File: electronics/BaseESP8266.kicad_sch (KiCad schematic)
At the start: 15 parts, among them P1 CONN_01X09, P2 CONN_01X09, SW1 Reset, T1 CONN_01X01, T2 CONN_01X01, U1 ESP-13-WROOM-02

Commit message: V2 Board needs: final traces, silkscreen and DRC
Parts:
- D5, D6: footprint mcqn-kicad-lib:LED_SMD_WL-SMSW_side-emitting -> LED_SMD:LED_0805_2012Metric_Pad1.15x1.40mm_HandSolder
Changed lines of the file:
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@@
       (effects (font (size 1.27 1.27)))
     )
-    (property "Footprint" "mcqn-kicad-lib:LED_SMD_WL-SMSW_side-emitting" (at 248.92 91.44 0)
+    (property "Footprint" "LED_SMD:LED_0805_2012Metric_Pad1.15x1.40mm_HandSolder" (at 248.92 91.44 0)
       (effects (font (size 1.27 1.27)) hide)
     )
@@
       (project "MyBikesGotLED"
         (path "/ea56fda8-6f8e-4826-a040-5c9b3e8e5cfa/00000000-0000-0000-0000-00005f8dad46"
-          (reference "D6") (unit 1) (value "LED") (footprint "mcqn-kicad-lib:LED_SMD_WL-SMSW_side-emitting")
+          (reference "D6") (unit 1) (value "LED") (footprint "LED_SMD:LED_0805_2012Metric_Pad1.15x1.40mm_HandSolder")
         )
       )
@@
       (effects (font (size 1.27 1.27)))
     )
-    (property "Footprint" "mcqn-kicad-lib:LED_SMD_WL-SMSW_side-emitting" (at 237.49 91.44 0)
+    (property "Footprint" "LED_SMD:LED_0805_2012Metric_Pad1.15x1.40mm_HandSolder" (at 237.49 91.44 0)
       (effects (font (size 1.27 1.27)) hide)
     )
@@
       (project "MyBikesGotLED"
         (path "/ea56fda8-6f8e-4826-a040-5c9b3e8e5cfa/00000000-0000-0000-0000-00005f8dad46"
-          (reference "D5") (unit 1) (value "LED") (footprint "mcqn-kicad-lib:LED_SMD_WL-SMSW_side-emitting")
+          (reference "D5") (unit 1) (value "LED") (footprint "LED_SMD:LED_0805_2012Metric_Pad1.15x1.40mm_HandSolder")
         )
       )

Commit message: V2 schematic - Battery management updates
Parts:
- renumbered C2 to C9, D5 to D1, D6 to D2, P1 to P3, P2 to P4, R9 to R12, R1 to R13, R2 to R14, R7 to R15, R8 to R16, R10 to R17, U1 to U4
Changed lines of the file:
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@@
-(kicad_sch (version 20221004) (generator eeschema)
+(kicad_sch (version 20221110) (generator eeschema)
   (paper "A4")
   (junction (at 144.78 57.15) (diameter 0) (color 0 0 0 0)
@@
   (symbol (lib_id "Device:R") (at 261.62 96.52 180) (unit 1)
     (in_bom yes) (on_board yes) (dnp no)
-    (property "Reference" "R10" (at 259.588 96.52 90)
+    (property "Reference" "R17" (at 259.588 96.52 90)
       (effects (font (size 1.27 1.27)))
     )
@@
       (project "MyBikesGotLED"
         (path "/ea56fda8-6f8e-4826-a040-5c9b3e8e5cfa/00000000-0000-0000-0000-00005f8dad46"
-          (reference "R10") (unit 1) (value "R10k") (footprint "Resistor_SMD:R_0603_1608Metric_Pad1.05x0.95mm_HandSolder")
+          (reference "R17") (unit 1) (value "R10k") (footprint "Resistor_SMD:R_0603_1608Metric_Pad1.05x0.95mm_HandSolder")
         )
       )
@@
   (symbol (lib_id "Device:C") (at 273.05 96.52 0) (unit 1)
     (in_bom yes) (on_board yes) (dnp no)
-    (property "Reference" "C2" (at 266.6492 96.52 90)
+    (property "Reference" "C9" (at 266.6492 96.52 90)
       (effects (font (size 1.27 1.27)))
     )
@@
       (project "MyBikesGotLED"
         (path "/ea56fda8-6f8e-4826-a040-5c9b3e8e5cfa/00000000-0000-0000-0000-00005f8dad46"
-          (reference "C2") (unit 1) (value "C47nF") (footprint "Capacitor_SMD:C_0603_1608Metric_Pad1.05x0.95mm_HandSolder")
+          (reference "C9") (unit 1) (value "C47nF") (footprint "Capacitor_SMD:C_0603_1608Metric_Pad1.05x0.95mm_HandSolder")
         )
       )
@@
   (symbol (lib_id "Device:R") (at 144.78 50.8 0) (unit 1)
     (in_bom yes) (on_board yes) (dnp no)
-    (property "Reference" "R9" (at 146.558 49.6316 0)
+    (property "Reference" "R12" (at 146.558 49.6316 0)
       (effects (font (size 1.27 1.27)) (justify left))
     )
@@
       (project "MyBikesGotLED"
         (path "/ea56fda8-6f8e-4826-a040-5c9b3e8e5cfa/00000000-0000-0000-0000-00005f8dad46"
-          (reference "R9") (unit 1) (value "R560") (footprint "Resistor_SMD:R_0603_1608Metric_Pad1.05x0.95mm_HandSolder")
+          (reference "R12") (unit 1) (value "R560") (footprint "Resistor_SMD:R_0603_1608Metric_Pad1.05x0.95mm_HandSolder")
         )
       )
@@
   (symbol (lib_id "Device:R") (at 248.92 101.6 180) (unit 1)
     (in_bom yes) (on_board yes) (dnp no)
-    (property "Reference" "R8" (at 246.888 101.6 90)
+    (property "Reference" "R16" (at 246.888 101.6 90)
       (effects (font (size 1.27 1.27)))
     )
@@
       (project "MyBikesGotLED"
         (path "/ea56fda8-6f8e-4826-a040-5c9b3e8e5cfa/00000000-0000-0000-0000-00005f8dad46"
-          (reference "R8") (unit 1) (value "R560") (footprint "Resistor_SMD:R_0603_1608Metric_Pad1.05x0.95mm_HandSolder")
+          (reference "R16") (unit 1) (value "R560") (footprint "Resistor_SMD:R_0603_1608Metric_Pad1.05x0.95mm_HandSolder")
         )
       )
@@
   (symbol (lib_id "Device:R") (at 237.49 101.6 180) (unit 1)
     (in_bom yes) (on_board yes) (dnp no)
-    (property "Reference" "R7" (at 235.458 101.6 90)
+    (property "Reference" "R15" (at 235.458 101.6 90)
       (effects (font (size 1.27 1.27)))
     )
@@
       (project "MyBikesGotLED"
         (path "/ea56fda8-6f8e-4826-a040-5c9b3e8e5cfa/00000000-0000-0000-0000-00005f8dad46"
-          (reference "R7") (unit 1) (value "R560") (footprint "Resistor_SMD:R_0603_1608Metric_Pad1.05x0.95mm_HandSolder")
+          (reference "R15") (unit 1) (value "R560") (footprint "Resistor_SMD:R_0603_1608Metric_Pad1.05x0.95mm_HandSolder")
         )
       )
@@
   (symbol (lib_id "Device:LED") (at 248.92 91.44 90) (unit 1)
     (in_bom yes) (on_board yes) (dnp no)
-    (property "Reference" "D6" (at 246.38 91.44 0)
+    (property "Reference" "D2" (at 246.38 91.44 0)
       (effects (font (size 1.27 1.27)))
     )
@@
       (project "MyBikesGotLED"
         (path "/ea56fda8-6f8e-4826-a040-5c9b3e8e5cfa/00000000-0000-0000-0000-00005f8dad46"
-          (reference "D6") (unit 1) (value "LED") (footprint "LED_SMD:LED_0805_2012Metric_Pad1.15x1.40mm_HandSolder")
+          (reference "D2") (unit 1) (value "LED") (footprint "LED_SMD:LED_0805_2012Metric_Pad1.15x1.40mm_HandSolder")
         )
       )
@@
   (symbol (lib_id "Device:LED") (at 237.49 91.44 90) (unit 1)
     (in_bom yes) (on_board yes) (dnp no)
-    (property "Reference" "D5" (at 234.95 91.44 0)
+    (property "Reference" "D1" (at 234.95 91.44 0)
       (effects (font (size 1.27 1.27)))
     )
@@
       (project "MyBikesGotLED"
         (path "/ea56fda8-6f8e-4826-a040-5c9b3e8e5cfa/00000000-0000-0000-0000-00005f8dad46"
-          (reference "D5") (unit 1) (value "LED") (footprint "LED_SMD:LED_0805_2012Metric_Pad1.15x1.40mm_HandSolder")
+          (reference "D1") (unit 1) (value "LED") (footprint "LED_SMD:LED_0805_2012Metric_Pad1.15x1.40mm_HandSolder")
         )
       )
@@
   (symbol (lib_id "Connector_Generic:Conn_01x09") (at 43.18 82.55 180) (unit 1)
     (in_bom yes) (on_board yes) (dnp no)
-    (property "Reference" "P1" (at 45.2374 66.675 0)
+    (property "Reference" "P3" (at 45.2374 66.675 0)
       (effects (font (size 1.27 1.27)))
     )
@@
       (project "MyBikesGotLED"
         (path "/ea56fda8-6f8e-4826-a040-5c9b3e8e5cfa/00000000-0000-0000-0000-00005f8dad46"
-          (reference "P1") (unit 1) (value "CONN_01X09") (footprint "Connector_PinSocket_2.54mm:PinSocket_1x09_P2.54mm_Vertical")
+          (reference "P3") (unit 1) (value "CONN_01X09") (footprint "Connector_PinSocket_2.54mm:PinSocket_1x09_P2.54mm_Vertical")
         )
       )
@@
   (symbol (lib_id "Connector_Generic:Conn_01x09") (at 92.71 82.55 0) (unit 1)
     (in_bom yes) (on_board yes) (dnp no)
-    (property "Reference" "P2" (at 94.6912 81.5086 0)
+    (property "Reference" "P4" (at 94.6912 81.5086 0)
       (effects (font (size 1.27 1.27)) (justify left))
     )
@@
       (project "MyBikesGotLED"
         (path "/ea56fda8-6f8e-4826-a040-5c9b3e8e5cfa/00000000-0000-0000-0000-00005f8dad46"
-          (reference "P2") (unit 1) (value "CONN_01X09") (footprint "Connector_PinSocket_2.54mm:PinSocket_1x09_P2.54mm_Vertical")
+          (reference "P4") (unit 1) (value "CONN_01X09") (footprint "Connector_PinSocket_2.54mm:PinSocket_1x09_P2.54mm_Vertical")
         )
       )
@@
   (symbol (lib_id "Device:R") (at 215.9 101.6 180) (unit 1)
     (in_bom yes) (on_board yes) (dnp no)
-    (property "Reference" "R1" (at 213.36 101.6 90)
+    (property "Reference" "R13" (at 213.36 101.6 90)
       (effects (font (size 1.27 1.27)))
     )
@@
       (project "MyBikesGotLED"
         (path "/ea56fda8-6f8e-4826-a040-5c9b3e8e5cfa/00000000-0000-0000-0000-00005f8dad46"
-          (reference "R1") (unit 1) (value "R10k") (footprint "Resistor_SMD:R_0603_1608Metric_Pad1.05x0.95mm_HandSolder")
+          (reference "R13") (unit 1) (value "R10k") (footprint "Resistor_SMD:R_0603_1608Metric_Pad1.05x0.95mm_HandSolder")
         )
       )
@@
   (symbol (lib_id "Device:R") (at 217.17 63.5 0) (unit 1)
     (in_bom yes) (on_board yes) (dnp no)
-    (property "Reference" "R2" (at 218.948 62.3316 0)
+    (property "Reference" "R14" (at 218.948 62.3316 0)
       (effects (font (size 1.27 1.27)) (justify left))
     )
@@
       (project "MyBikesGotLED"
         (path "/ea56fda8-6f8e-4826-a040-5c9b3e8e5cfa/00000000-0000-0000-0000-00005f8dad46"
-          (reference "R2") (unit 1) (value "R10k") (footprint "Resistor_SMD:R_0603_1608Metric_Pad1.05x0.95mm_HandSolder")
+          (reference "R14") (unit 1) (value "R10k") (footprint "Resistor_SMD:R_0603_1608Metric_Pad1.05x0.95mm_HandSolder")
         )
       )
@@
   (symbol (lib_id "RF_Module:ESP-WROOM-02") (at 171.45 81.28 0) (unit 1)
     (in_bom yes) (on_board yes) (dnp no)
-    (property "Reference" "U1" (at 170.815 61.849 0)
+    (property "Reference" "U4" (at 170.815 61.849 0)
       (effects (font (size 1.27 1.27)))
     )
@@
       (project "MyBikesGotLED"
         (path "/ea56fda8-6f8e-4826-a040-5c9b3e8e5cfa/00000000-0000-0000-0000-00005f8dad46"
-          (reference "U1") (unit 1) (value "ESP-13-WROOM-02") (footprint "RF_Module:ESP-WROOM-02")
-        )
-      )
+          (reference "U4") (unit 1) (value "ESP-13-WROOM-02") (footprint "RF_Module:ESP-WROOM-02")
+        )
+      )

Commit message: Boost circuit moved and extra copper added
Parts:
- C9: footprint Capacitor_SMD:C_0603_1608Metric_Pad1.05x0.95mm_HandSolder -> Capacitor_SMD:C_0603_1608Metric_Pad1.08x0.95mm_HandSolder
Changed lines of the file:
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@@
       (effects (font (size 1.27 1.27)))
     )
-    (property "Footprint" "Capacitor_SMD:C_0603_1608Metric_Pad1.05x0.95mm_HandSolder" (at 274.0152 100.33 0)
+    (property "Footprint" "Capacitor_SMD:C_0603_1608Metric_Pad1.08x0.95mm_HandSolder" (at 274.0152 100.33 0)
       (effects (font (size 1.27 1.27)) hide)
     )
@@
       (project "MyBikesGotLED"
         (path "/ea56fda8-6f8e-4826-a040-5c9b3e8e5cfa/00000000-0000-0000-0000-00005f8dad46"
-          (reference "C9") (unit 1) (value "C47nF") (footprint "Capacitor_SMD:C_0603_1608Metric_Pad1.05x0.95mm_HandSolder")
+          (reference "C9") (unit 1) (value "C47nF") (footprint "Capacitor_SMD:C_0603_1608Metric_Pad1.08x0.95mm_HandSolder")
         )
       )

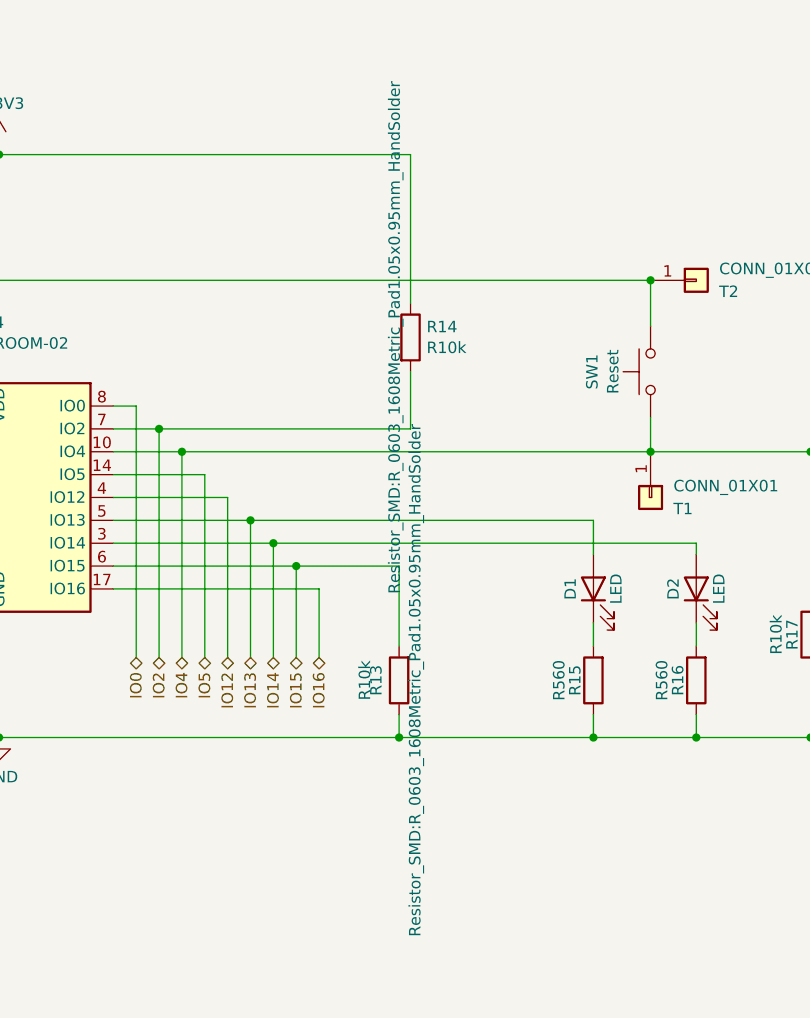
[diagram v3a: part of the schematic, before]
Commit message: All componets placed and silk screen tidied
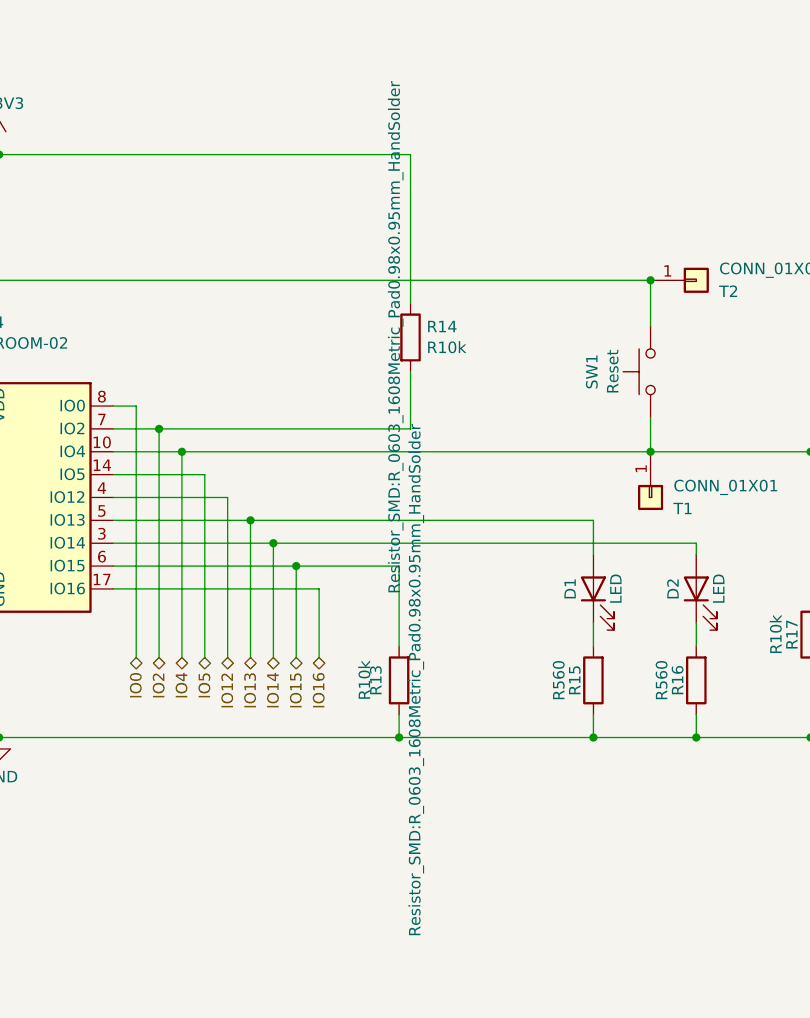
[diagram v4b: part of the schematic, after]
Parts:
- R12, R13, R14, R15, R16, R17: footprint Resistor_SMD:R_0603_1608Metric_Pad1.05x0.95mm_HandSolder -> Resistor_SMD:R_0603_1608Metric_Pad0.98x0.95mm_HandSolder
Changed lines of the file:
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@@
       (effects (font (size 1.27 1.27)))
     )
-    (property "Footprint" "Resistor_SMD:R_0603_1608Metric_Pad1.05x0.95mm_HandSolder" (at 263.398 96.52 90)
+    (property "Footprint" "Resistor_SMD:R_0603_1608Metric_Pad0.98x0.95mm_HandSolder" (at 263.398 96.52 90)
       (effects (font (size 1.27 1.27)) hide)
     )
@@
       (project "MyBikesGotLED"
         (path "/ea56fda8-6f8e-4826-a040-5c9b3e8e5cfa/00000000-0000-0000-0000-00005f8dad46"
-          (reference "R17") (unit 1) (value "R10k") (footprint "Resistor_SMD:R_0603_1608Metric_Pad1.05x0.95mm_HandSolder")
+          (reference "R17") (unit 1) (value "R10k") (footprint "Resistor_SMD:R_0603_1608Metric_Pad0.98x0.95mm_HandSolder")
         )
       )
@@
       (effects (font (size 1.27 1.27)) (justify left))
     )
-    (property "Footprint" "Resistor_SMD:R_0603_1608Metric_Pad1.05x0.95mm_HandSolder" (at 143.002 50.8 90)
+    (property "Footprint" "Resistor_SMD:R_0603_1608Metric_Pad0.98x0.95mm_HandSolder" (at 143.002 50.8 90)
       (effects (font (size 1.27 1.27)) hide)
     )
@@
       (project "MyBikesGotLED"
         (path "/ea56fda8-6f8e-4826-a040-5c9b3e8e5cfa/00000000-0000-0000-0000-00005f8dad46"
-          (reference "R12") (unit 1) (value "R560") (footprint "Resistor_SMD:R_0603_1608Metric_Pad1.05x0.95mm_HandSolder")
+          (reference "R12") (unit 1) (value "R560") (footprint "Resistor_SMD:R_0603_1608Metric_Pad0.98x0.95mm_HandSolder")
         )
       )
@@
       (effects (font (size 1.27 1.27)))
     )
-    (property "Footprint" "Resistor_SMD:R_0603_1608Metric_Pad1.05x0.95mm_HandSolder" (at 250.698 101.6 90)
+    (property "Footprint" "Resistor_SMD:R_0603_1608Metric_Pad0.98x0.95mm_HandSolder" (at 250.698 101.6 90)
       (effects (font (size 1.27 1.27)) hide)
     )
@@
       (project "MyBikesGotLED"
         (path "/ea56fda8-6f8e-4826-a040-5c9b3e8e5cfa/00000000-0000-0000-0000-00005f8dad46"
-          (reference "R16") (unit 1) (value "R560") (footprint "Resistor_SMD:R_0603_1608Metric_Pad1.05x0.95mm_HandSolder")
+          (reference "R16") (unit 1) (value "R560") (footprint "Resistor_SMD:R_0603_1608Metric_Pad0.98x0.95mm_HandSolder")
         )
       )
@@
       (effects (font (size 1.27 1.27)))
     )
-    (property "Footprint" "Resistor_SMD:R_0603_1608Metric_Pad1.05x0.95mm_HandSolder" (at 239.268 101.6 90)
+    (property "Footprint" "Resistor_SMD:R_0603_1608Metric_Pad0.98x0.95mm_HandSolder" (at 239.268 101.6 90)
       (effects (font (size 1.27 1.27)) hide)
     )
@@
       (project "MyBikesGotLED"
         (path "/ea56fda8-6f8e-4826-a040-5c9b3e8e5cfa/00000000-0000-0000-0000-00005f8dad46"
-          (reference "R15") (unit 1) (value "R560") (footprint "Resistor_SMD:R_0603_1608Metric_Pad1.05x0.95mm_HandSolder")
+          (reference "R15") (unit 1) (value "R560") (footprint "Resistor_SMD:R_0603_1608Metric_Pad0.98x0.95mm_HandSolder")
         )
       )
@@
       (effects (font (size 1.27 1.27)))
     )
-    (property "Footprint" "Resistor_SMD:R_0603_1608Metric_Pad1.05x0.95mm_HandSolder" (at 217.678 101.6 90)
+    (property "Footprint" "Resistor_SMD:R_0603_1608Metric_Pad0.98x0.95mm_HandSolder" (at 217.678 101.6 90)
       (effects (font (size 1.27 1.27)))
     )
@@
       (project "MyBikesGotLED"
         (path "/ea56fda8-6f8e-4826-a040-5c9b3e8e5cfa/00000000-0000-0000-0000-00005f8dad46"
-          (reference "R13") (unit 1) (value "R10k") (footprint "Resistor_SMD:R_0603_1608Metric_Pad1.05x0.95mm_HandSolder")
+          (reference "R13") (unit 1) (value "R10k") (footprint "Resistor_SMD:R_0603_1608Metric_Pad0.98x0.95mm_HandSolder")
         )
       )
@@
       (effects (font (size 1.27 1.27)) (justify left))
     )
-    (property "Footprint" "Resistor_SMD:R_0603_1608Metric_Pad1.05x0.95mm_HandSolder" (at 215.392 63.5 90)
+    (property "Footprint" "Resistor_SMD:R_0603_1608Metric_Pad0.98x0.95mm_HandSolder" (at 215.392 63.5 90)
       (effects (font (size 1.27 1.27)))
     )
@@
       (project "MyBikesGotLED"
         (path "/ea56fda8-6f8e-4826-a040-5c9b3e8e5cfa/00000000-0000-0000-0000-00005f8dad46"
-          (reference "R14") (unit 1) (value "R10k") (footprint "Resistor_SMD:R_0603_1608Metric_Pad1.05x0.95mm_HandSolder")
-        )
-      )
+          (reference "R14") (unit 1) (value "R10k") (footprint "Resistor_SMD:R_0603_1608Metric_Pad0.98x0.95mm_HandSolder")
+        )
+      )

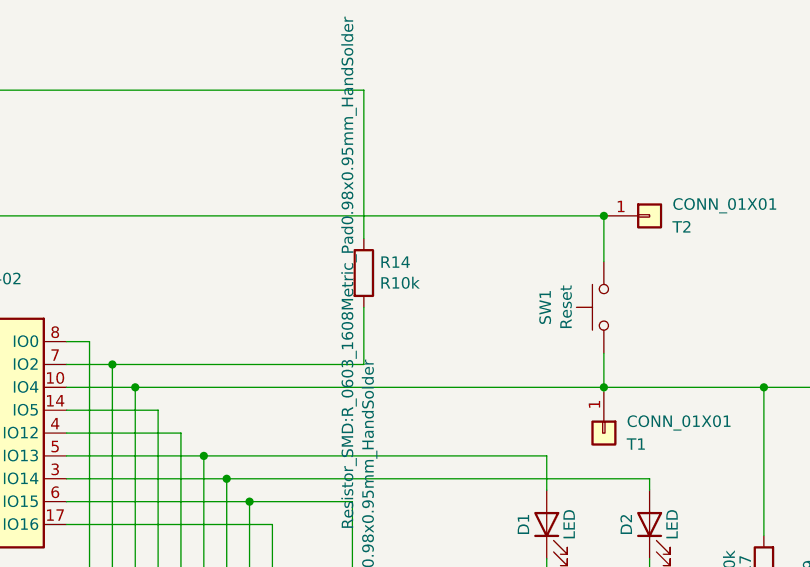
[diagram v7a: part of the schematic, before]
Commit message: Updated schematic meta and BOM
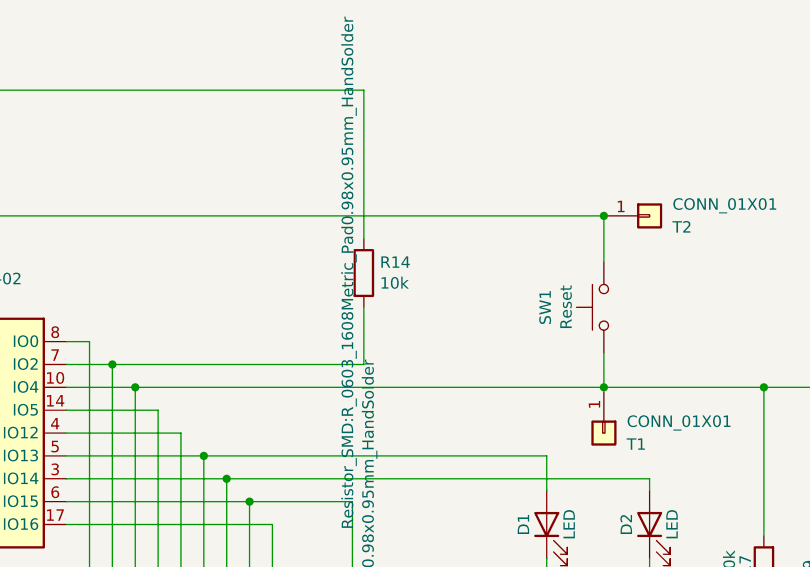
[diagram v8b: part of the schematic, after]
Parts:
- R14: value R10k -> 10k
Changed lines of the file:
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@@
       (effects (font (size 1.27 1.27)) (justify left))
     )
-    (property "Value" "R10k" (at 218.948 64.643 0)
+    (property "Value" "10k" (at 218.948 64.643 0)
       (effects (font (size 1.27 1.27)) (justify left))
     )
@@
       (project "MyBikesGotLED"
         (path "/ea56fda8-6f8e-4826-a040-5c9b3e8e5cfa/00000000-0000-0000-0000-00005f8dad46"
-          (reference "R14") (unit 1) (value "R10k") (footprint "Resistor_SMD:R_0603_1608Metric_Pad0.98x0.95mm_HandSolder")
+          (reference "R14") (unit 1) (value "10k") (footprint "Resistor_SMD:R_0603_1608Metric_Pad0.98x0.95mm_HandSolder")
         )
       )
@@
       (effects (font (size 1.524 1.524)) hide)
     )
+    (property "Description" "ESP-WROOM-02 free issue" (at 171.45 81.28 0)
+      (effects (font (size 1.27 1.27)) hide)
+    )
     (pin "1")
